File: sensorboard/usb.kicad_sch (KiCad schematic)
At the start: 27 parts

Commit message: schemtiac update
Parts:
- gave numbers to parts that had none: 27

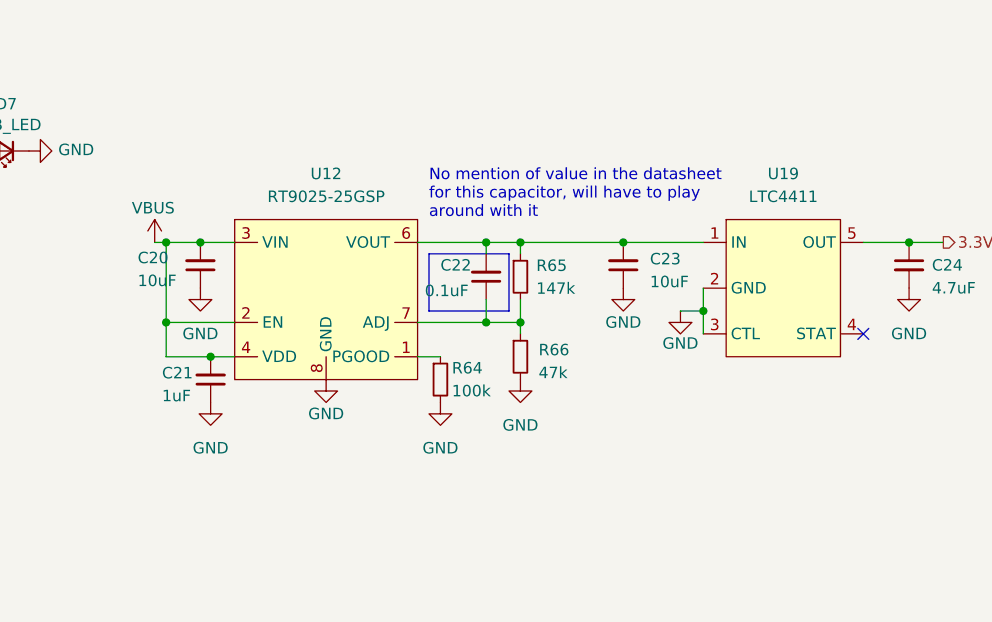
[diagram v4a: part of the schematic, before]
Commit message: updated boost converter schematic, 5V lines
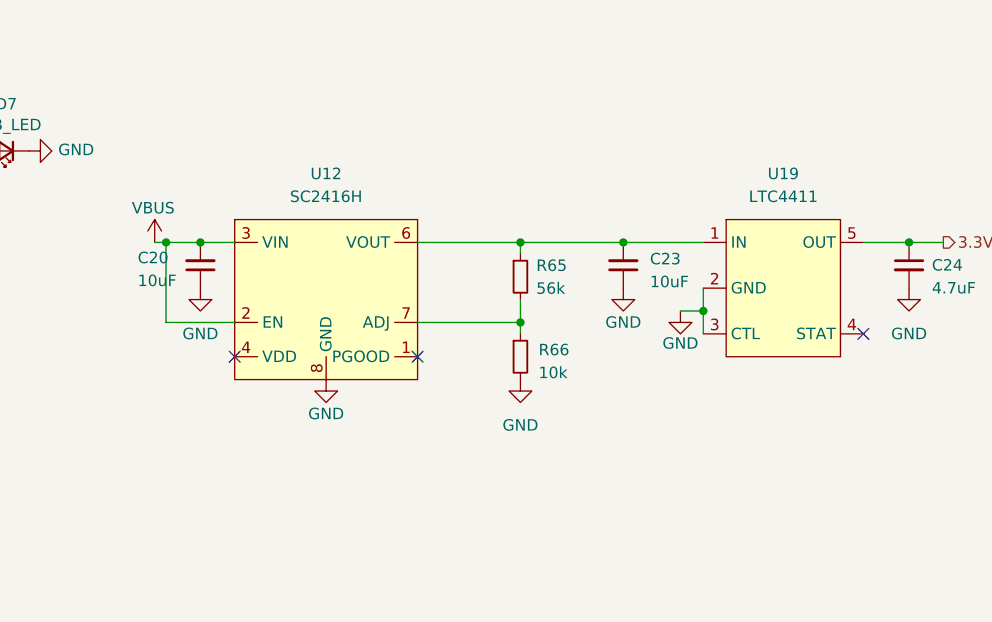
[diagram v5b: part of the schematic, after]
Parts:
- removed C21: 1uF, Capacitor_SMD:C_0603_1608Metric, symbol Device:C_Small
- removed C22: 0.1uF, Capacitor_SMD:C_0603_1608Metric, symbol Device:C_Small
- removed R64: 100k, Resistor_SMD:R_0603_1608Metric, symbol Device:R_Small
- R65: value 147k -> 56k
- R66: value 47k -> 10k
- U12: value RT9025-25GSP -> SC2416H; footprint Package_SO:SOP-8_3.9x4.9mm_P1.27mm -> iclr:SOIC127P599X175-9N
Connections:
- net VBUS: no longer U12.4 (VDD)
- no-connect marks 21 -> 23
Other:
- note removed: "No mention of value in the datasheet for this capacitor, will have to play around with it"

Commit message: added silkscreens and fixed LNA_IN line
fixed labels for TPs and LEDs
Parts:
- renumbered TP25 to Data+_TP1, TP24 to Data-_TP1, D7 to USB_LED2, TP26 to VBUS_TP1
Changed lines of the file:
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@@
   (symbol (lib_id "Connector:TestPoint") (at 43.18 107.95 270) (unit 1)
     (in_bom yes) (on_board yes)
-    (property "Reference" "TP25" (id 0) (at 47.9552 106.7816 90)
+    (property "Reference" "Data+_TP1" (id 0) (at 47.9552 106.7816 90)
       (effects (font (size 1.27 1.27)) (justify left))
     )
@@
   (symbol (lib_id "Device:LED_Small") (at 153.67 96.52 180) (unit 1)
     (in_bom yes) (on_board yes)
-    (property "Reference" "D7" (id 0) (at 153.67 91.313 0))
+    (property "Reference" "USB_LED2" (id 0) (at 153.67 91.313 0))
     (property "Value" "USB_LED" (id 1) (at 153.67 93.6244 0))
     (property "Footprint" "LED_SMD:LED_0603_1608Metric" (id 2) (at 153.67 96.52 90)
@@
   (symbol (lib_id "Connector:TestPoint") (at 43.18 113.03 270) (unit 1)
     (in_bom yes) (on_board yes)
-    (property "Reference" "TP26" (id 0) (at 47.9552 111.8616 90)
+    (property "Reference" "VBUS_TP1" (id 0) (at 47.9552 111.8616 90)
       (effects (font (size 1.27 1.27)) (justify left))
     )
@@
   (symbol (lib_id "Connector:TestPoint") (at 43.18 102.87 270) (unit 1)
     (in_bom yes) (on_board yes)
-    (property "Reference" "TP24" (id 0) (at 47.9552 101.7016 90)
-      (effects (font (size 1.27 1.27)) (justify left))
-    )
+    (property "Reference" "Data-_TP1" (id 0) (at 47.9552 101.7016 90)
+      (effects (font (size 1.27 1.27)) (justify left))
+    )

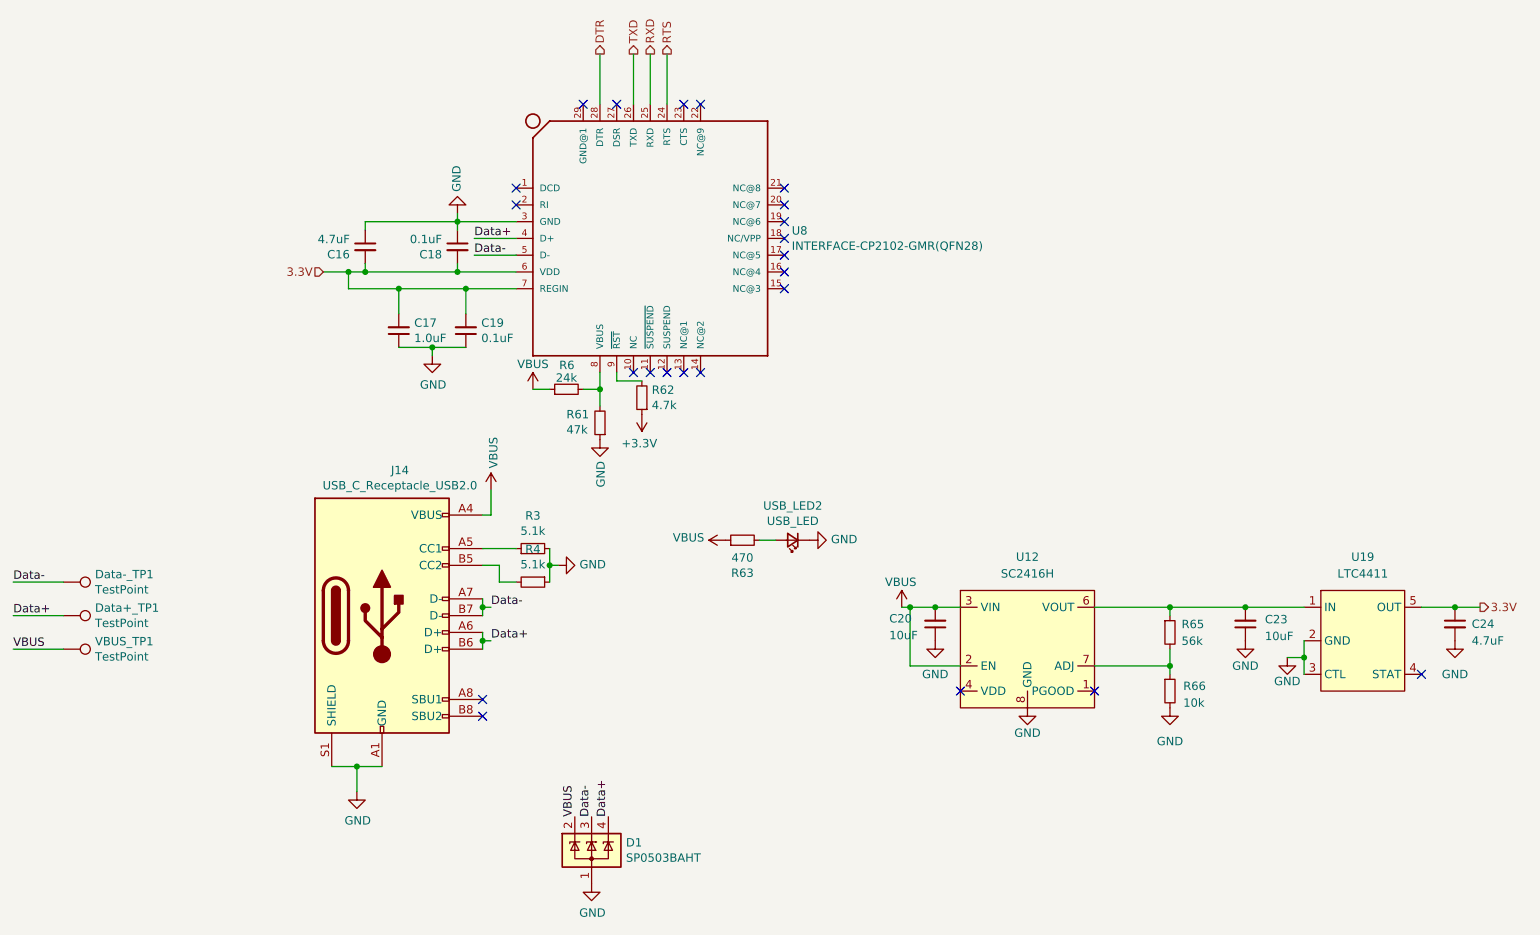
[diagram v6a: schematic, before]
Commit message: Connected LDO and CP2102 EPs to GND, expanded U.FL keepout
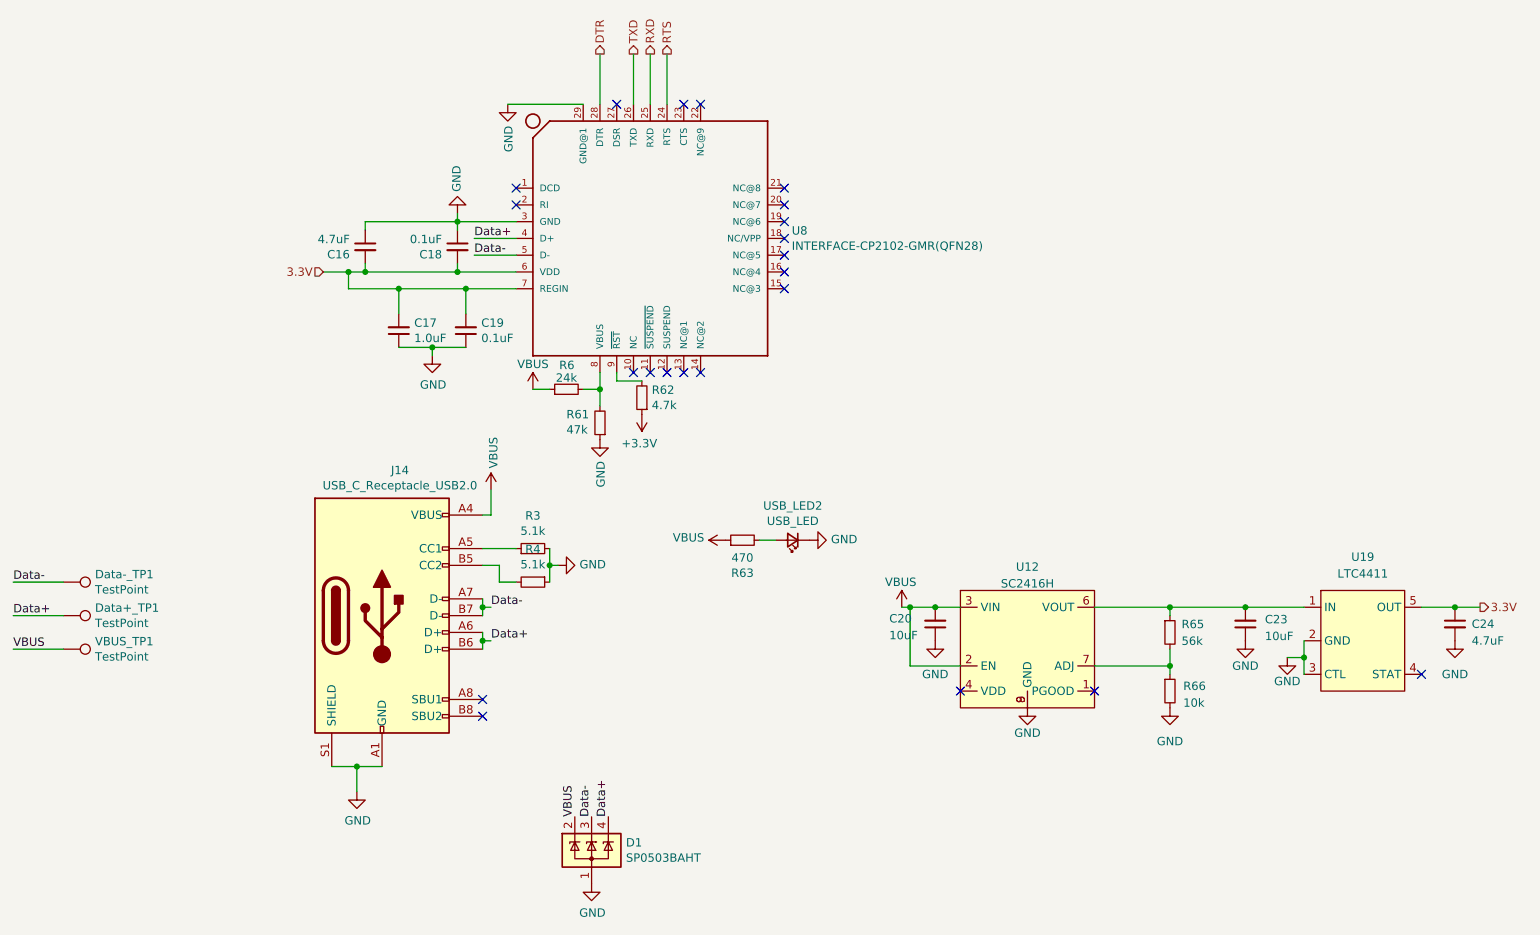
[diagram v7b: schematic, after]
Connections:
- net GND: now also U12.9 (GND), U8.29 (GND@1)
- no-connect marks 23 -> 22
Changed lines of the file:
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@@
   (no_connect (at 137.16 71.12))
   (no_connect (at 129.54 71.12))
-  (no_connect (at 121.92 30.48))
   (no_connect (at 111.76 45.72))
   (no_connect (at 111.76 43.18))
@@
   )
   (wire (pts (xy 87.63 130.81) (xy 91.44 130.81))
+    (stroke (width 0) (type default) (color 0 0 0 0))
+  )
+  (wire (pts (xy 110.49 30.48) (xy 121.92 30.48))
     (stroke (width 0) (type default) (color 0 0 0 0))
   )
@@
   (symbol (lib_id "iclr:RT9025-25GSP") (at 189.23 105.41 0) (unit 1)
     (in_bom yes) (on_board yes) (fields_autoplaced)
-    (property "Reference" "U12" (id 0) (at 189.23 99.06 0))
-    (property "Value" "SC2416H" (id 1) (at 189.23 101.6 0))
+    (property "Reference" "U12" (id 0) (at 189.23 100.5672 0))
+    (property "Value" "SC2416H" (id 1) (at 189.23 103.1041 0))
     (property "Footprint" "iclr:SOIC127P599X175-9N" (id 2) (at 189.23 100.33 0)
       (effects (font (size 1.27 1.27)) hide)
@@
     (pin "7")
     (pin "8")
+    (pin "9")
   )
   (symbol (lib_id "power:VBUS") (at 170.18 106.68 0) (unit 1)
@@
       (effects (font (size 1.27 1.27)) hide)
     )
+    (pin "1")
+  )
+  (symbol (lib_id "power:GND") (at 110.49 30.48 0) (unit 1)
+    (in_bom yes) (on_board yes)
+    (property "Reference" "#PWR0160" (id 0) (at 110.49 36.83 0)
+      (effects (font (size 1.27 1.27)) hide)
+    )
+    (property "Value" "GND" (id 1) (at 110.617 33.7312 90)
+      (effects (font (size 1.27 1.27)) (justify right))
+    )
+    (property "Footprint" "" (id 2) (at 110.49 30.48 0)
+      (effects (font (size 1.27 1.27)) hide)
+    )
+    (property "Datasheet" "" (id 3) (at 110.49 30.48 0)
+      (effects (font (size 1.27 1.27)) hide)
+    )
